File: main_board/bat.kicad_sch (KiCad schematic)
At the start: 36 parts, among them IC1 MP2722GRH-0000-Z, IC2 MP3429GL-Z, IC3 NX3DV42GU, J4 USB_B_Micro, J5 USB_C_Receptacle_USB2.0, U3 ATmega32U4-M, Y1 Crystal

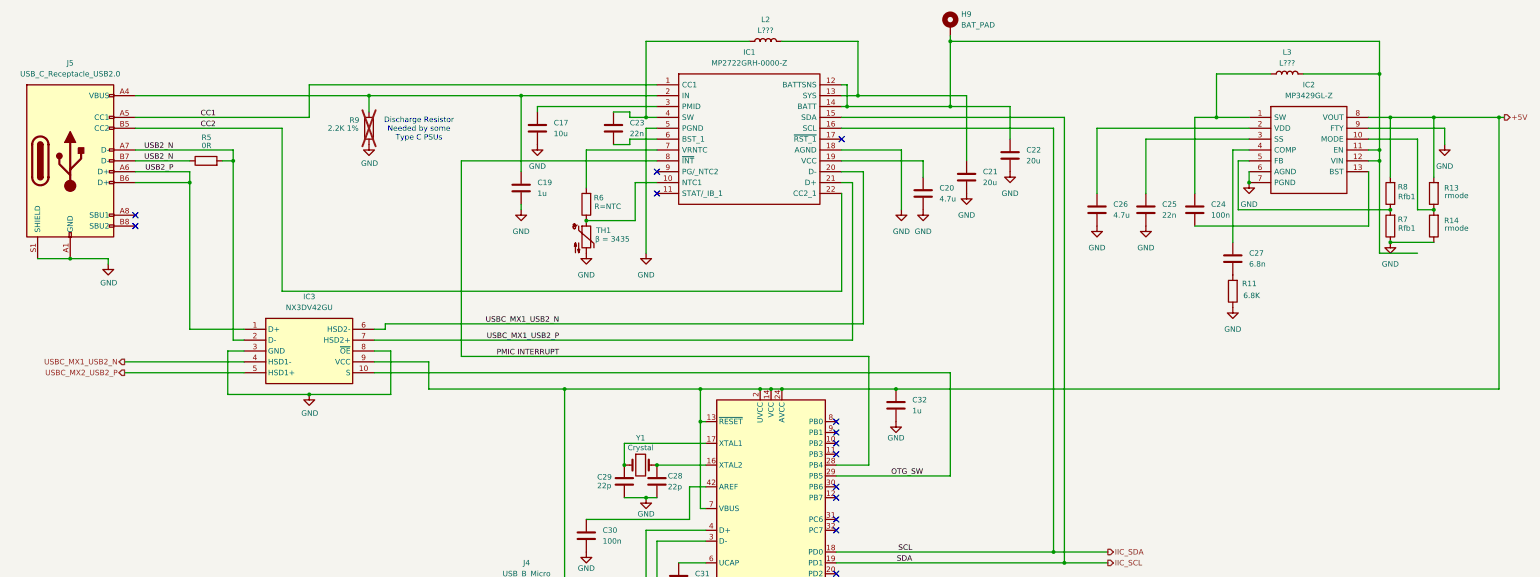
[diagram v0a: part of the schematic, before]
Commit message: Implement part of power management.
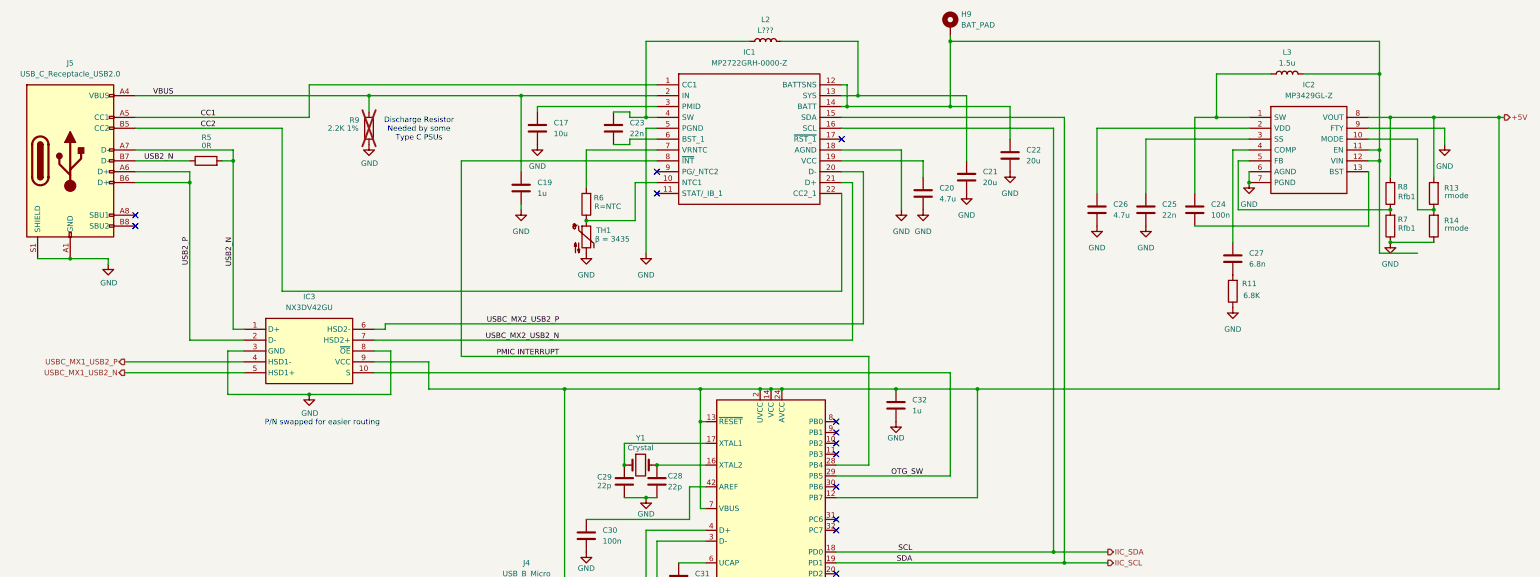
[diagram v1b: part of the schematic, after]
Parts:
- C17, C19, C20, C21, C22, C23, C24, C25, C26, C27, C28, C29, C30, C31, C32: footprint (none) -> Capacitor_SMD:C_0805_2012Metric_Pad1.18x1.45mm_HandSolder
- H9: footprint (none) -> TestPoint:TestPoint_Pad_4.0x4.0mm
- IC1: footprint MP2722GRH0000Z -> 000_custom:MP2722GRH0000Z
- IC2: footprint MP3431GLP -> 000_custom:MP3431GLP
- IC3: footprint NX3DV42GU -> 000_custom:NX3DV42GU
- J4: footprint (none) -> Connector_USB:USB_Micro-B_Amphenol_10104110_Horizontal
- L2: footprint (none) -> Inductor_SMD:L_Bourns_SRP1038C_10.0x10.0mm
- L3: value L??? -> 1.5u; footprint (none) -> Inductor_SMD:L_Bourns_SRP1038C_10.0x10.0mm
- TH1: footprint (none) -> Resistor_SMD:R_0805_2012Metric_Pad1.20x1.40mm_HandSolder
- Y1: footprint (none) -> Crystal:Crystal_SMD_5032-4Pin_5.0x3.2mm
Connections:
- net +5V: now also U3.12 (PB7)
- net USB2_N: now also IC3.1 (D+); no longer IC3.2 (D-)
- net USB2_P: now also IC3.2 (D-); no longer IC3.1 (D+)
- net USBC_MX1_USB2_N: now also IC3.5 (HSD1+); no longer IC1.20 (D-), IC3.4 (HSD1-), IC3.6 (HSD2-)
- net USBC_MX1_USB2_P: now also IC3.4 (HSD1-); no longer IC1.21 (D+), IC3.7 (HSD2+)
- net USBC_MX2_USB2_P: now also IC1.20 (D-), IC3.6 (HSD2-); no longer IC3.5 (HSD1+)
- net VBUS: now reaches C19.1, IC1.2 (IN), J5.A4 (VBUS), J5.A9 (VBUS), J5.B4 (VBUS), J5.B9 (VBUS), R9.1
- new net USBC_MX2_USB2_N: IC1.21 (D+), IC3.7 (HSD2+)
- no-connect marks 27 -> 26
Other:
- note added: "P/N swapped for easier routing"

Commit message: More power management goodness
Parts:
- removed R13, R14: rmode, Resistor_SMD:R_0805_2012Metric_Pad1.20x1.40mm_HandSolder, symbol Device:R
- added C33, C34, C35, C36, C37, C38: 22u, Capacitor_SMD:C_0805_2012Metric_Pad1.18x1.45mm_HandSolder, symbol Device:C
- added C39: 100n, Capacitor_SMD:C_0805_2012Metric_Pad1.18x1.45mm_HandSolder, symbol Device:C
- added R17: 15K, Resistor_SMD:R_0805_2012Metric_Pad1.20x1.40mm_HandSolder, symbol Device:R
- added SW1: Right angle Tact button, Button_Switch_SMD:SW_Push_1P1T_NO_CK_KSC7xxJ, symbol Switch:SW_Push
- J5: footprint Library:USB421603A -> 000_custom:USB421603A
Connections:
- net +5V: now also C36.1, C37.1, C38.1, C39.1; no longer C32.2, IC3.9 (VCC), J4.1 (VBUS), U3.12 (PB7), U3.13 (~{RESET}), U3.14 (VCC), U3.2 (UVCC), U3.24 (AVCC), U3.34 (VCC), U3.44 (AVCC), U3.7 (VBUS)
- net GND: now also C33.2, C34.2, C35.2, C36.2, C37.2, C38.2, C39.2, SW1.1
- net V_SYS: now reaches C21.1, IC1.13 (SYS), L2.2
- net V_SYS: now also C32.2, IC3.9 (VCC), J4.1 (VBUS), U3.12 (PB7), U3.13 (~{RESET}), U3.14 (VCC), U3.2 (UVCC), U3.24 (AVCC), U3.34 (VCC), U3.44 (AVCC), U3.7 (VBUS)
- net VBAT: now reaches C22.1, H9.MP, IC1.12 (BATTSNS), IC1.14 (BATT), IC2.12 (VIN), L3.2
- net VBAT: now also C33.1, C34.1, C35.1, R17.2; no longer IC2.11 (EN)
- net at U3.11 (PB3): now also IC2.11 (EN), R17.1
- net VBUS renamed VIN
- no-connect marks 26 -> 27
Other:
- moved on the sheet: C28, C29, C30, C31, C32, J4, R15, R16, R7, R8, U3, Y1

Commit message: Finalize power management
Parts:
- added C41: 100n, Capacitor_SMD:C_0805_2012Metric_Pad1.18x1.45mm_HandSolder, symbol Device:C
- added IC4: AP2204R-3.3TRG1, AP2204R33TRG1, symbol 000_Custom:AP2204R-3.3TRG1
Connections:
- net GND: now also R17.1, C41.1, IC4.2 (GND_1), IC4.4 (GND_2)
- net IIC_SCL: now also IC1.16 (SCL), U3.18 (PD0); no longer IC1.15 (SDA), U3.19 (PD1)
- net IIC_SDA: now also IC1.15 (SDA), U3.19 (PD1); no longer IC1.16 (SCL), U3.18 (PD0)
- net USBC_MX1_USB2_N: now also IC3.7 (HSD2+); no longer IC3.5 (HSD1+)
- net USBC_MX1_USB2_P: now also IC3.6 (HSD2-); no longer IC3.4 (HSD1-)
- net USBC_MX2_USB2_N: now also IC3.4 (HSD1-); no longer IC3.7 (HSD2+)
- net USBC_MX2_USB2_P: now also IC3.5 (HSD1+); no longer IC3.6 (HSD2-)
- net V_SYS: now also IC4.1 (VIN); no longer C32.2, IC3.9 (VCC), J4.1 (VBUS), U3.12 (PB7), U3.13 (~{RESET}), U3.14 (VCC), U3.2 (UVCC), U3.24 (AVCC), U3.34 (VCC), U3.44 (AVCC), U3.7 (VBUS)
- net at IC2.11 (EN), U3.11 (PB3): no longer R17.1
- net CM5_PMIC_EN: now reaches U3.30 (PB6)
- new net PMIC_3.3V: C32.2, C41.2, IC3.9 (VCC), IC4.3 (VOUT), J4.1 (VBUS), U3.12 (PB7), U3.13 (~{RESET}), U3.14 (VCC), U3.2 (UVCC), U3.24 (AVCC), U3.34 (VCC), U3.44 (AVCC), U3.7 (VBUS)
- no-connect marks 27 -> 26
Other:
- moved on the sheet: C17, C19, C20, C21, C22, C23, C24, C25, C26, C27, C28, C29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

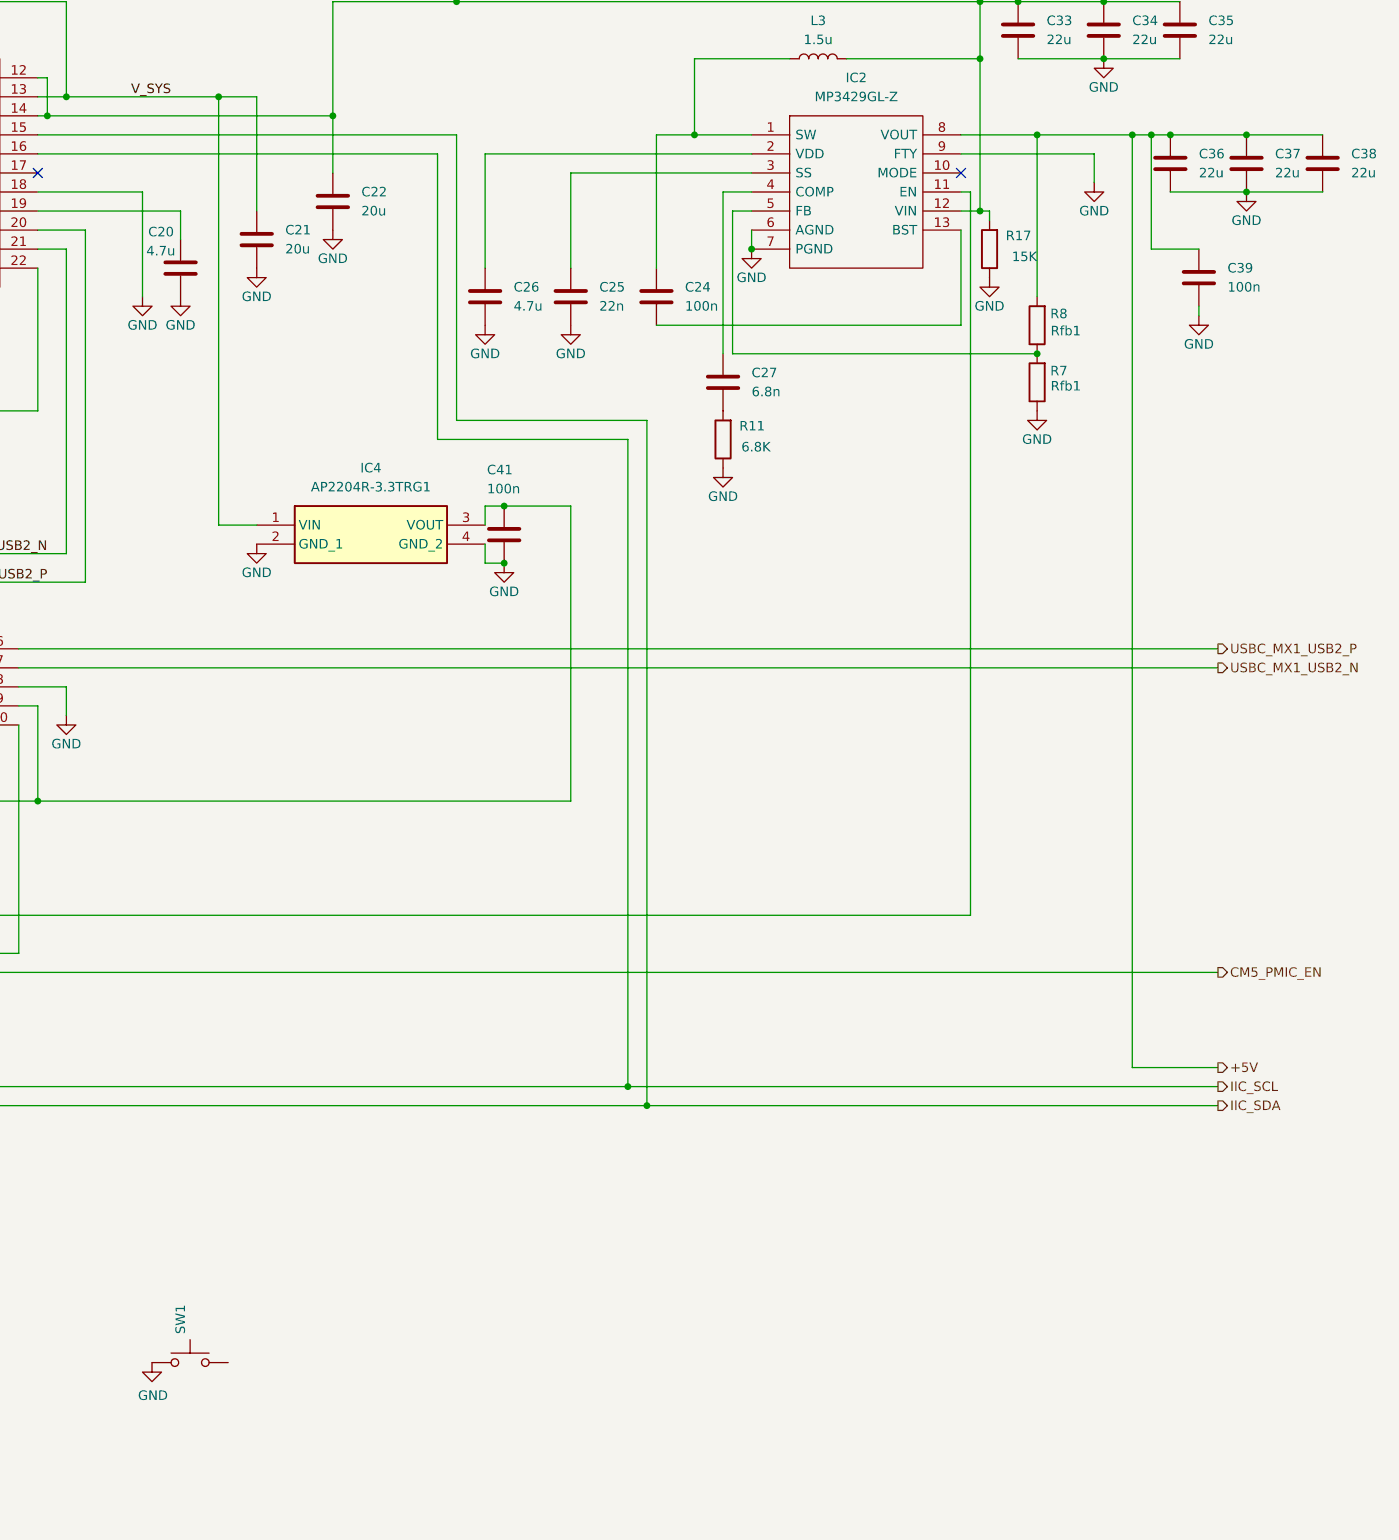
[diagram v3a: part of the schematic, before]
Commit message: Start reouting USB hub
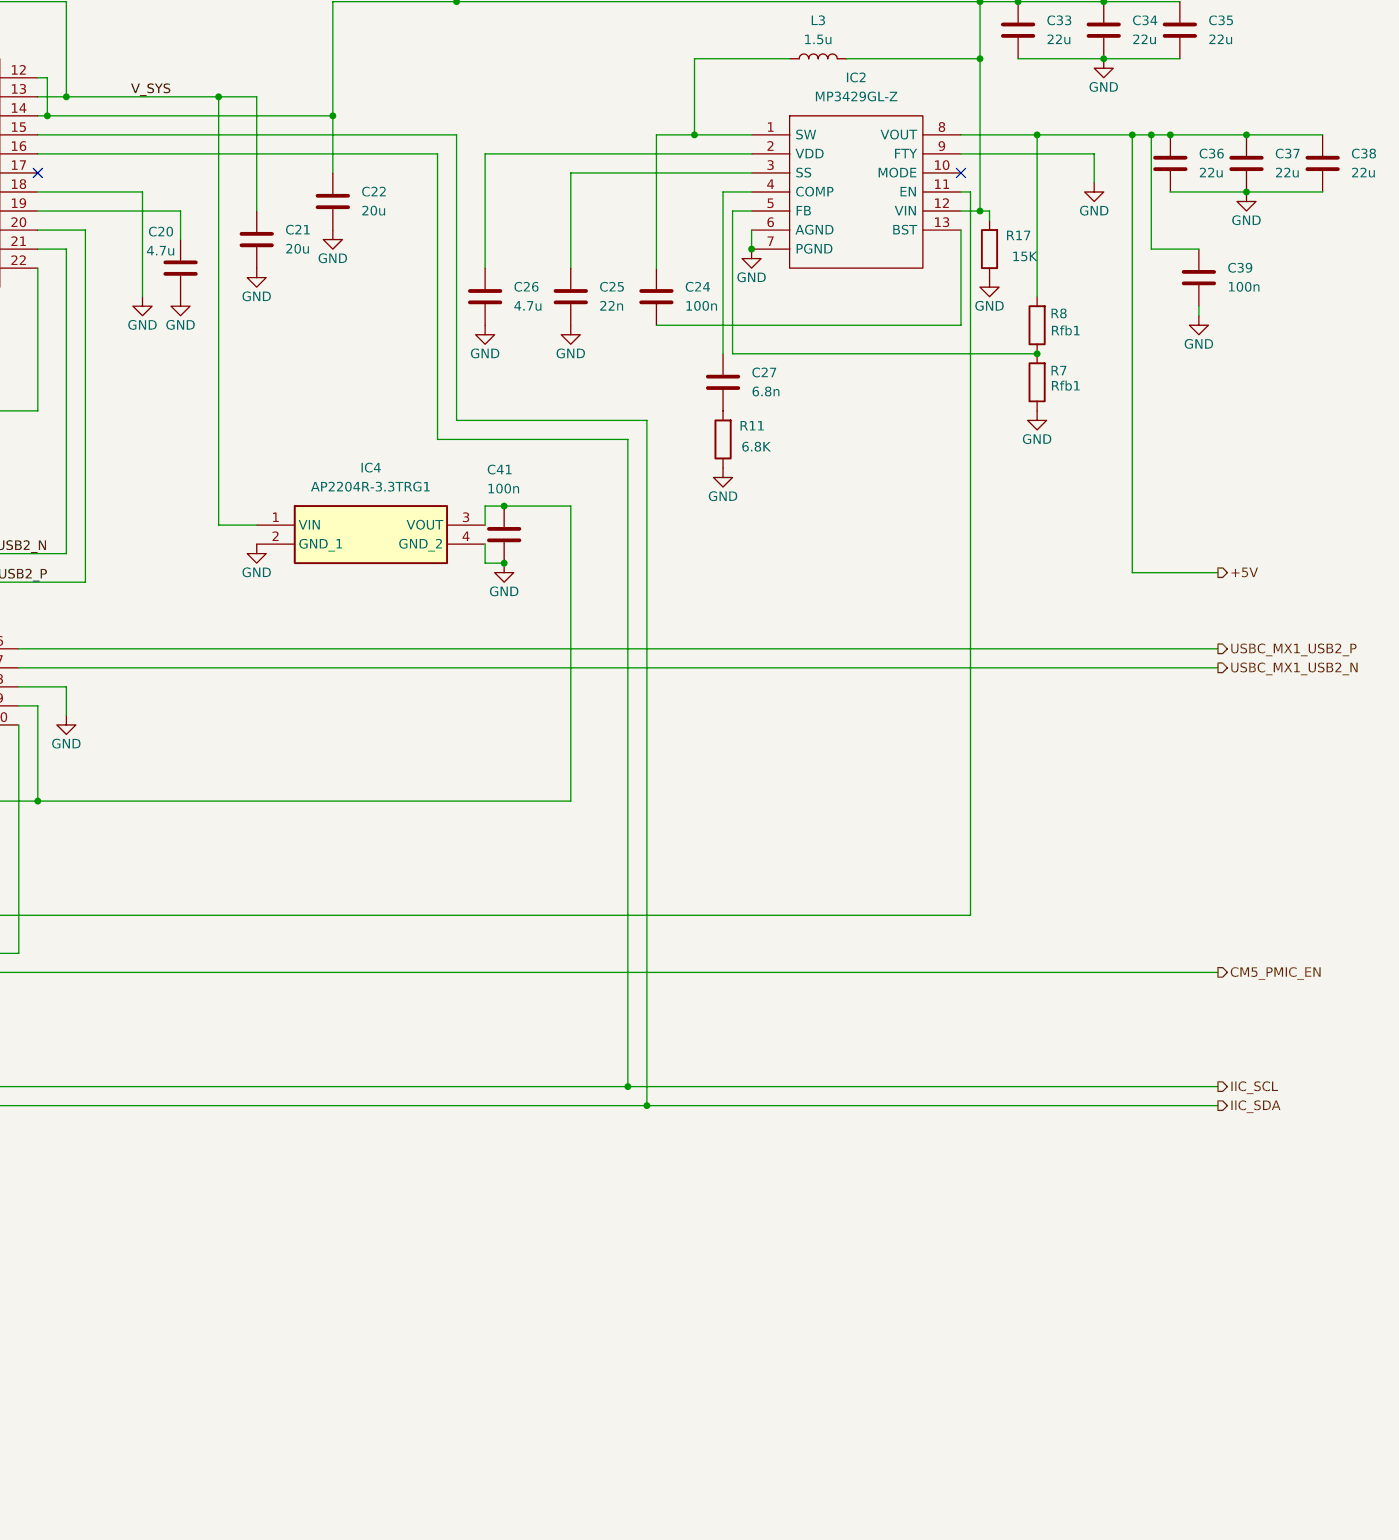
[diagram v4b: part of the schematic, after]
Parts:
- removed SW1: Right angle Tact button, Button_Switch_SMD:SW_Push_1P1T_NO_CK_KSC7xxJ, symbol Switch:SW_Push
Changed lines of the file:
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@@
 	(wire
 		(pts
-			(xy 369.57 185.42) (xy 381 185.42)
+			(xy 369.57 119.38) (xy 381 119.38)
 		)
 		(stroke
@@
 	(wire
 		(pts
-			(xy 369.57 60.96) (xy 369.57 185.42)
+			(xy 369.57 60.96) (xy 369.57 119.38)
 		)
 		(stroke
@@
 	(hierarchical_label "+5V"
 		(shape output)
-		(at 381 185.42 0)
+		(at 381 119.38 0)
 		(fields_autoplaced yes)
 		(effects
@@
 	)
 	(symbol
-		(lib_id "Switch:SW_Push")
-		(at 243.84 224.79 0)
-		(unit 1)
-		(exclude_from_sim no)
-		(in_bom yes)
-		(on_board yes)
-		(dnp no)
-		(property "Reference" "SW1"
-			(at 242.5699 220.98 90)
-			(effects
-				(font
-					(size 1.27 1.27)
-				)
-				(justify left)
-			)
-		)
-		(property "Value" "Right angle Tact button"
-			(at 245.364 220.98 90)
-			(effects
-				(font
-					(size 1.27 1.27)
-				)
-				(justify left)
-				(hide yes)
-			)
-		)
-		(property "Footprint" "Button_Switch_SMD:SW_Push_1P1T_NO_CK_KSC7xxJ"
-			(at 243.84 219.71 0)
-			(effects
-				(font
-					(size 1.27 1.27)
-				)
-				(hide yes)
-			)
-		)
-		(property "Datasheet" "https://www.mouser.co.uk/datasheet/2/240/Littelfuse-3050591.pdf"
-			(at 243.84 219.71 0)
-			(effects
-				(font
-					(size 1.27 1.27)
-				)
-				(hide yes)
-			)
-		)
-		(property "Description" "Push button switch, generic, two pins"
-			(at 243.84 224.79 0)
-			(effects
-				(font
-					(size 1.27 1.27)
-				)
-				(hide yes)
-			)
-		)
-		(property "Field5" "PTS645VH58-2LFS"
-			(at 243.84 224.79 0)
-			(effects
-				(font
-					(size 1.27 1.27)
-				)
-				(hide yes)
-			)
-		)
-		(property "Field6" "PTS645VH58-2LFS"
-			(at 243.84 224.79 0)
-			(effects
-				(font
-					(size 1.27 1.27)
-				)
-				(hide yes)
-			)
-		)
-		(property "Field7" "CK"
-			(at 243.84 224.79 0)
-			(effects
-				(font
-					(size 1.27 1.27)
-				)
-				(hide yes)
-			)
-		)
-		(property "Part Description" "Right angle through hole Tact switch"
-			(at 243.84 224.79 0)
-			(effects
-				(font
-					(size 1.27 1.27)
-				)
-				(hide yes)
-			)
-		)
-		(pin "1"
-		)
-		(pin "2"
-		)
-		(instances
-			(project "main_board"
-				(path "/e63e39d7-6ac0-4ffd-8aa3-1841a4541b55/b84f1a66-243e-4389-abcf-18bc380f8da3"
-					(reference "SW1")
-					(unit 1)
-				)
-			)
-		)
-	)
-	(symbol
 		(lib_id "Device:C")
 		(at 52.07 171.45 0)
@@
 					(unit 1)
 				)
-			)
-		)
-	)
-	(symbol
-		(lib_id "power:GND")
-		(at 238.76 224.79 0)
-		(unit 1)
-		(exclude_from_sim no)
-		(in_bom yes)
-		(on_board yes)
-		(dnp no)
-		(property "Reference" "#PWR030"
-			(at 238.76 231.14 0)
-			(effects
-				(font
-					(size 1.27 1.27)
-				)
-				(hide yes)
-			)
-		)
-		(property "Value" "GND"
-			(at 238.887 229.1842 0)
-			(effects
-				(font
-					(size 1.27 1.27)
-				)
-			)
-		)
-		(property "Footprint" ""
-			(at 238.76 224.79 0)
-			(effects
-				(font
-					(size 1.27 1.27)
-				)
-				(hide yes)
-			)
-		)
-		(property "Datasheet" ""
-			(at 238.76 224.79 0)
-			(effects
-				(font
-					(size 1.27 1.27)
-				)
-				(hide yes)
-			)
-		)
-		(property "Description" "Power symbol creates a global label with name \"GND\" , ground"
-			(at 238.76 224.79 0)
-			(effects
-				(font
-					(size 1.27 1.27)
-				)
-				(hide yes)
-			)
-		)
-		(pin "1"
-		)
-		(instances
-			(project "main_board"
-				(path "/e63e39d7-6ac0-4ffd-8aa3-1841a4541b55/b84f1a66-243e-4389-abcf-18bc380f8da3"
-					(reference "#PWR030")
-					(unit 1)
-				)
